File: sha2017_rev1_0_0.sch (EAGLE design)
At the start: 205 parts, among them IC1 CP210X_USB_UART, IC2 AP7215, IC3 ESP32WROOM32, IC4 TP4056, IC5 FXL6408, IC6 CPT112, M1 MOTOR10MM, Q1 MMBT2222A, Q2 MMBT2222A, Q3 MMBT2222A, Q4 MMBT2222A, Q5 SI1304 BDL, Q6 MMBT2222A, T1 MOSFET-PCHANNEL, T2 MOSFET-PCHANNEL, T3 MOSFET-PCHANNEL, X2 2908-05WB-MG, X4 JST-PH3

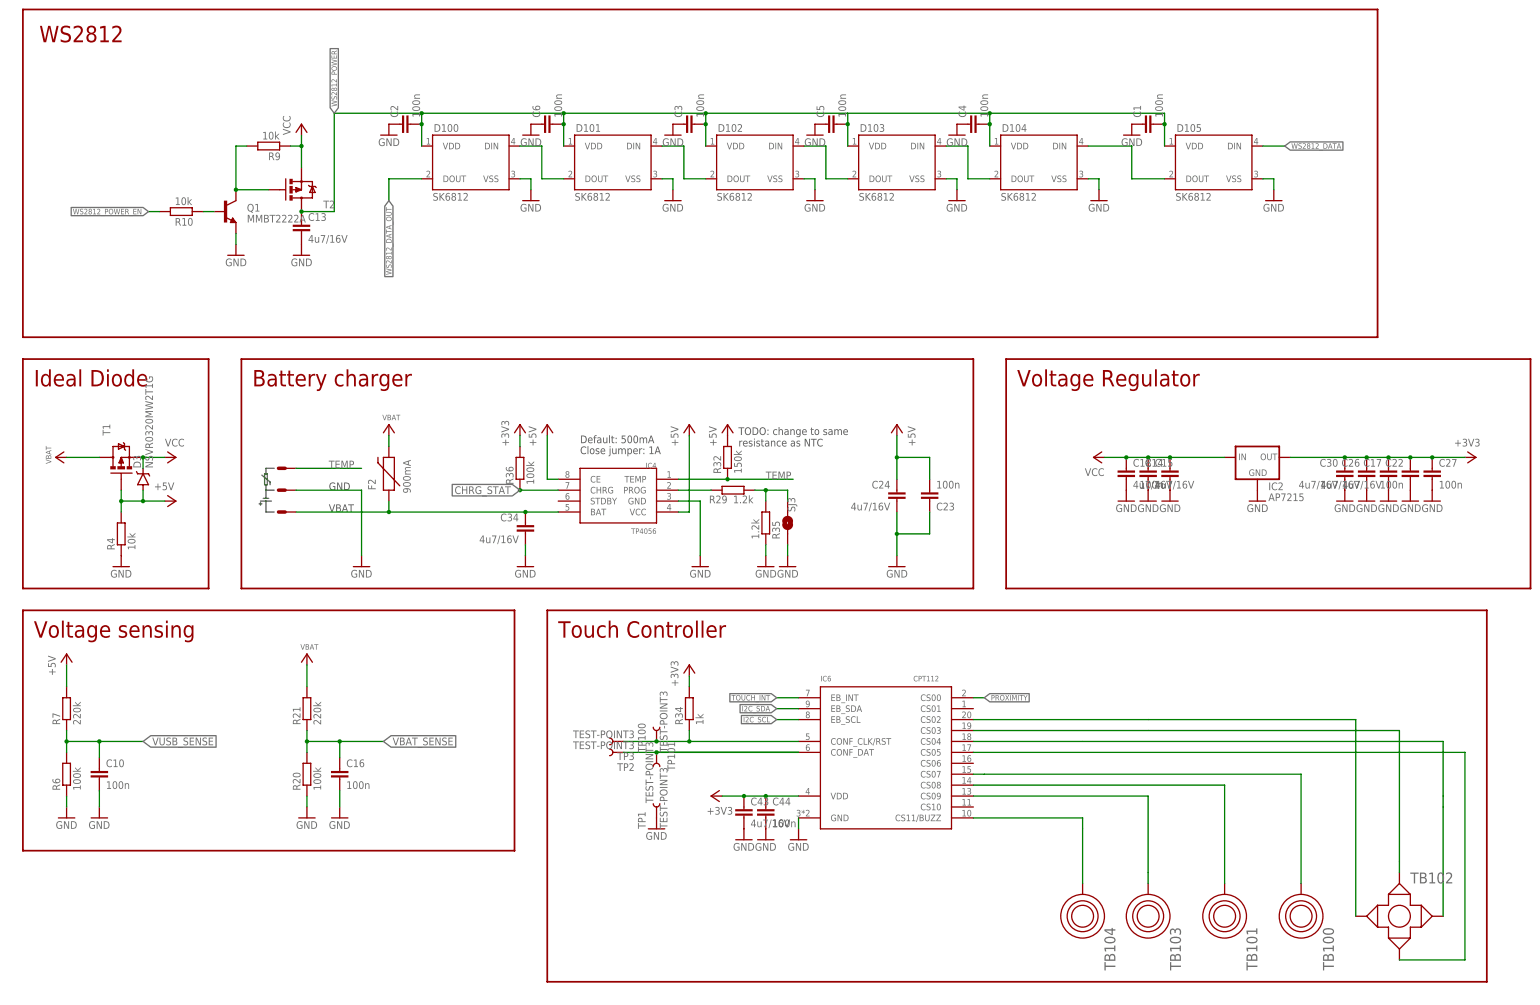
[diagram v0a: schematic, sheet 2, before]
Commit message: Swap port expander and CPT112S for MPR121
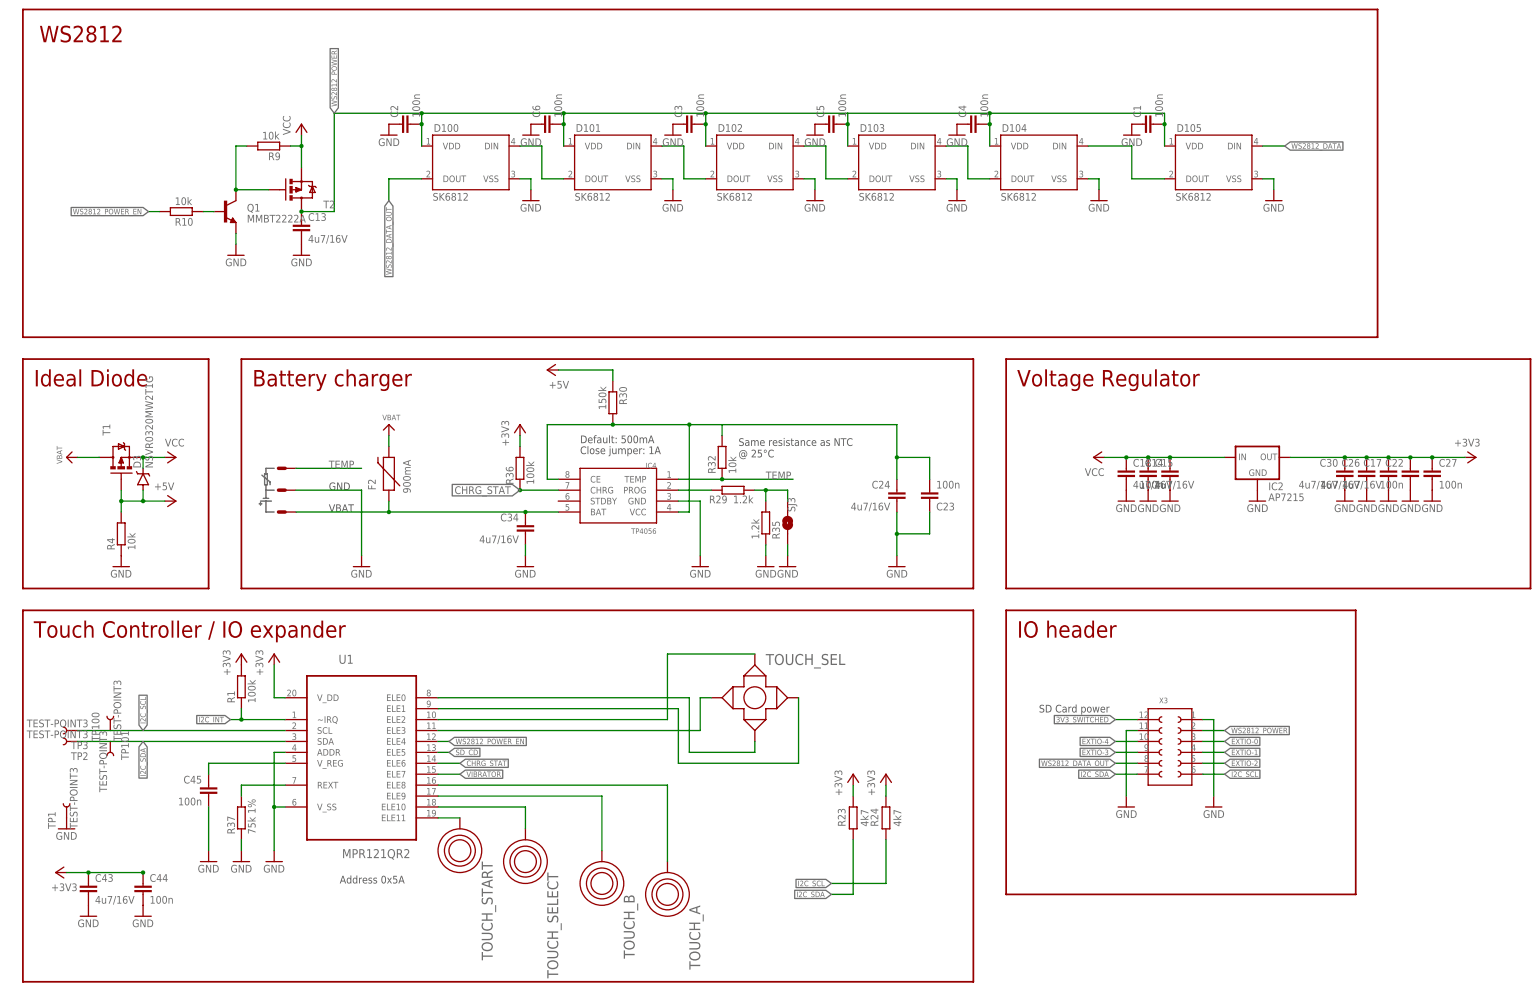
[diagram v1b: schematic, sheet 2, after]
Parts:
- removed C42: 100n, sha2017_rev0_1_0_dev:C0603-DASHES
- removed IC5: FXL6408, badge:FXL6408
- removed IC6: CPT112, badge:CPT112
- removed R26, R33: 10k, sha2017_rev0_1_0_dev:R0603-DASHES
- removed R34: 1k, sha2017_rev0_1_0_dev:R0603-DASHES
- removed SJ1, SJ2: JUMPER-PAD-2-NOYES_SILK, SparkFun-Passives:JUMPER-PAD-2-NOYES_SILK
- removed TB100, TB101: TOUCHSELECT, badge:TOUCHSELECT
- removed TB102: TOUCH_CROSS, badge:TOUCH_CROSS
- removed TB103, TB104: TOUCHROUND, badge:TOUCHROUND
- added C45: 100n, sha2017_rev0_1_0_dev:C0603-DASHES
- added R30: 150k, sha2017_rev0_1_0_dev:R0603-DASHES
- added R37: 75k 1%, sha2017_rev0_1_0_dev:R0603-DASHES
- added TOUCH_A, TOUCH_B: TOUCHROUND, badge:TOUCHROUND
- added TOUCH_SEL: TOUCH_CROSS, badge:TOUCH_CROSS
- added TOUCH_SELECT, TOUCH_START: TOUCHSELECT, badge:TOUCHSELECT
- added U1: MPR121QR2, Freescale_By_element14_Batch_1:MPR121QR2
- R1: value 10k -> 100k; device 00ralf:R0603-DASHES -> sha2017_rev0_1_0_dev:R0603-DASHES; PARTNO ERJ-3GEYJ103V -> ERJ-3GEYJ104V
- R32: value 150k -> 10k
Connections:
- removed net EXTIO-5: IC5.GPIO5, X3.2
- removed net N$55: IC6.CS03, TB102.UP
- removed net N$57: IC6.CS05, TB102.DOWN
- removed net N$58: IC6.CS09, TB103.P$1
- removed net N$59: IC5.!RESET, R33.2
- removed net N$61: IC6.CONF_CLK/RST, R34.1, TP100.1, TP3.1
- removed net N$62: IC6.CONF_DAT, TP101.1, TP2.1
- removed net N$64: IC6.CS08, TB101.P$1
- removed net N$65: IC6.CS07, TB100.P$1
- removed net PROXIMITY: IC6.CS00
- removed net SD_DATA1: IC3.IO4, R1.1, SJ2.1
- removed net SD_DATA2: IC3.IO12, SJ1.1
- removed net SD_DATA2_OUT: R26.1, SJ1.2, X2.NC
- removed net TOUCH_INT: IC5.GPIO3, IC6.EB_INT
- new net N$12: C23.2, C24.1, IC4.CE, IC4.VCC, R30.2, R32.2
- new net N$20: C45.1, U1.V_REG
- new net N$21: R37.2, U1.REXT
- new net N$24: TOUCH_B.P$1, U1.ELE9
- new net N$44: TOUCH_SEL.DOWN, U1.ELE0
- new net N$46: TOUCH_SELECT.P$1, U1.ELE10
- new net N$47: TOUCH_SEL.UP, U1.ELE2
- net +3V3: now also R1.2, U1.V_DD; no longer C42.1, IC5.ADDR, IC5.VCC, IC5.VDDIO, IC6.VDD, R33.1, R34.2
- net +5V: now also R30.1; no longer C23.2, C24.1, IC4.CE, IC4.VCC, R32.2
- net 3V3_SWITCHED: no longer R1.2, R26.2
- net CHRG_STAT: now also U1.ELE6; no longer IC5.GPIO0
- net EXTIO-3: now also IC3.IO4; no longer IC5.GPIO7
- net EXTIO-4: now also IC3.IO12; no longer IC5.GPIO6
- net GND: now also C45.2, R37.1, U1.ADDR, U1.V_SS, X3.2; no longer C42.2, IC5.GND, IC6.GND
- net I2C_INT: now also R1.1, U1.~IRQ; no longer IC5.INT
- net I2C_SCL: now also TP100.1, TP3.1, U1.SCL; no longer IC5.SCL, IC6.EB_SCL
- net I2C_SDA: now also TP101.1, TP2.1, U1.SDA; no longer IC5.SDA, IC6.EB_SDA
- net N$1: now also TOUCH_A.P$1, U1.ELE8; no longer IC6.CS11/BUZZ, TB104.P$1
- net N$25: now also TOUCH_SEL.LEFT, U1.ELE3; no longer IC6.CS02, TB102.LEFT
- net N$56: now also TOUCH_SEL.RIGHT, U1.ELE1; no longer IC6.CS04, TB102.RIGHT
- net N$6: now also TOUCH_START.P$1, U1.ELE11; no longer SJ2.2, X2.RSV
- net SD_CD: now also U1.ELE5; no longer IC5.GPIO4
- net VIBRATOR: now also U1.ELE7; no longer IC5.GPIO1
- net WS2812_POWER_EN: now also U1.ELE4; no longer IC5.GPIO2
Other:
- note added: "Address 0x5A"
- note added: "DAT1"
- note added: "DAT2"
- note added: "SD Card power"
- note added: "Same resistance as NTC @ 25°C"
- note added: "Touch Controller / IO expander"
- note removed: "Port Expander"
- note removed: "TODO: change to same resistance as NTC"
- note removed: "Touch Controller"
- moved on the sheet: C43, C44, M1, Q2, R11, R2, R31, R32, TP1, TP100, TP101, TP2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

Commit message: Replace BJTs by AO3400 nFET
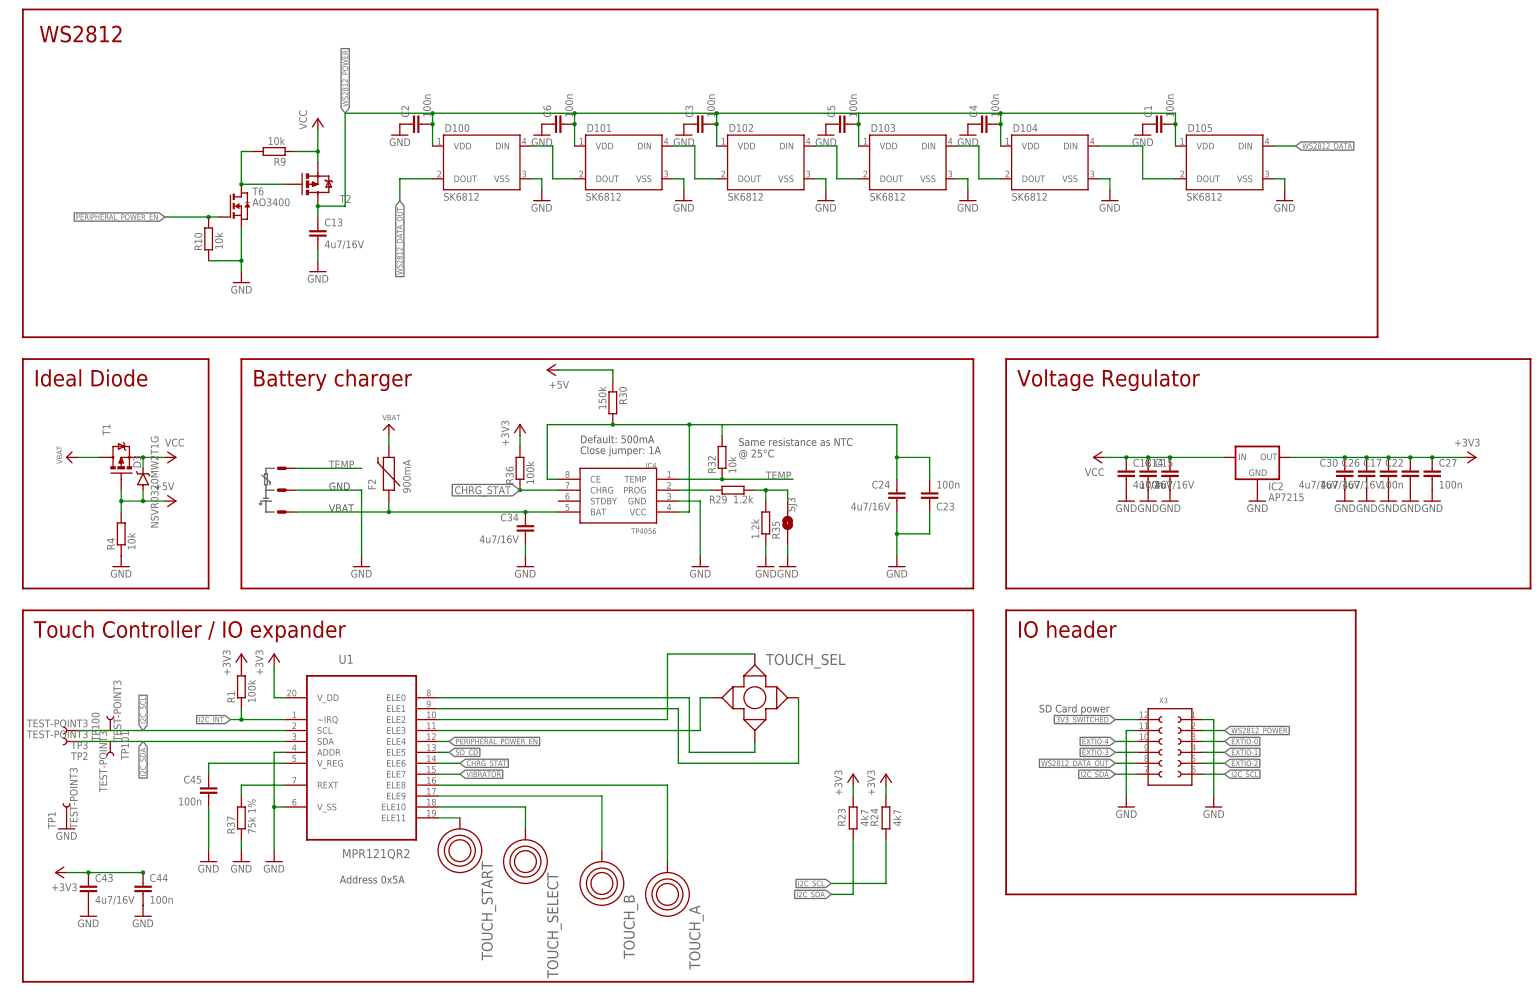
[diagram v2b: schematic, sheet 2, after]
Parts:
- removed Q1, Q2, Q6: MMBT2222A, SparkFun-DiscreteSemi:TRANSISTOR_NPNMMBT2222A
- added T4, T5, T6: AO3400, zetex:NMOSSOT23
- R11, R27: value 10k -> 100k
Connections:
- removed net N$15: Q6.B, R27.2
- removed net N$45: Q2.B, R11.1
- removed net N$52: Q1.B, R10.2
- removed net WS2812_POWER_EN: R10.1, R27.1, U1.ELE4
- new net PERIPHERAL_POWER_EN: R10.1, R27.2, T5.G, T6.G, U1.ELE4
- net GND: now also R10.2, R11.2, R27.1, T4.S, T5.S, T6.S; no longer Q1.E, Q2.E, Q6.E
- net N$16: now also T4.D; no longer Q2.C
- net N$17: now also T5.D; no longer Q6.C
- net N$53: now also T6.D; no longer Q1.C
- net VIBRATOR: now also R11.1, T4.G; no longer R11.2
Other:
- moved on the sheet: C1, C13, C2, C3, C4, C5, C6, D100, D101, D102, D103, D104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

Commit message: Fix r10
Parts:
- R4: value 10k -> 100k
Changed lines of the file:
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@@
 <setting verticaltext="up"/>
 </settings>
-<grid distance="0.05" unitdist="inch" unit="inch" style="lines" multiple="1" display="no" altdistance="0.01" altunitdist="inch" altunit="inch"/>
+<grid distance="0.1" unitdist="inch" unit="inch" style="lines" multiple="1" display="no" altdistance="0.01" altunitdist="inch" altunit="inch"/>
 <layers>
-<layer number="1" name="Top" color="4" fill="1" visible="yes" active="no"/>
-<layer number="2" name="Route2" color="1" fill="3" visible="yes" active="no"/>
-<layer number="3" name="Route3" color="4" fill="3" visible="yes" active="no"/>
-<layer number="4" name="Route4" color="1" fill="4" visible="yes" active="no"/>
-<layer number="5" name="Route5" color="4" fill="4" visible="yes" active="no"/>
-<layer number="6" name="Route6" color="1" fill="8" visible="yes" active="no"/>
-<layer number="7" name="Route7" color="4" fill="8" visible="yes" active="no"/>
-<layer number="8" name="Route8" color="1" fill="2" visible="yes" active="no"/>
-<layer number="9" name="Route9" color="4" fill="2" visible="yes" active="no"/>
-<layer number="10" name="Route10" color="1" fill="7" visible="yes" active="no"/>
-<layer number="11" name="Route11" color="4" fill="7" visible="yes" active="no"/>
-<layer number="12" name="Route12" color="1" fill="5" visible="yes" active="no"/>
-<layer number="13" name="Route13" color="4" fill="5" visible="yes" active="no"/>
-<layer number="14" name="Route14" color="1" fill="6" visible="yes" active="no"/>
-<layer number="15" name="Route15" color="4" fill="6" visible="yes" active="no"/>
-<layer number="16" name="Bottom" color="1" fill="1" visible="yes" active="no"/>
-<layer number="17" name="Pads" color="2" fill="1" visible="yes" active="no"/>
-<layer number="18" name="Vias" color="2" fill="1" visible="yes" active="no"/>
-<layer number="19" name="Unrouted" color="6" fill="1" visible="yes" active="no"/>
-<layer number="20" name="Dimension" color="15" fill="1" visible="yes" active="no"/>
-<layer number="21" name="tPlace" color="7" fill="1" visible="yes" active="no"/>
-<layer number="22" name="bPlace" color="7" fill="1" visible="yes" active="no"/>
-<layer number="23" name="tOrigins" color="15" fill="1" visible="yes" active="no"/>
-<layer number="24" name="bOrigins" color="15" fill="1" visible="yes" active="no"/>
-<layer number="25" name="tNames" color="7" fill="1" visible="yes" active="no"/>
-<layer number="26" name="bNames" color="7" fill="1" visible="yes" active="no"/>
-<layer number="27" name="tValues" color="7" fill="1" visible="yes" active="no"/>
-<layer number="28" name="bValues" color="7" fill="1" visible="yes" active="no"/>
+<layer number="1" name="Top" color="4" fill="1" visible="no" active="no"/>
+<layer number="2" name="Route2" color="1" fill="3" visible="no" active="no"/>
+<layer number="3" name="Route3" color="4" fill="3" visible="no" active="no"/>
+<layer number="4" name="Route4" color="1" fill="4" visible="no" active="no"/>
+<layer number="5" name="Route5" color="4" fill="4" visible="no" active="no"/>
+<layer number="6" name="Route6" color="1" fill="8" visible="no" active="no"/>
+<layer number="7" name="Route7" color="4" fill="8" visible="no" active="no"/>
+<layer number="8" name="Route8" color="1" fill="2" visible="no" active="no"/>
+<layer number="9" name="Route9" color="4" fill="2" visible="no" active="no"/>
+<layer number="10" name="Route10" color="1" fill="7" visible="no" active="no"/>
+<layer number="11" name="Route11" color="4" fill="7" visible="no" active="no"/>
+<layer number="12" name="Route12" color="1" fill="5" visible="no" active="no"/>
+<layer number="13" name="Route13" color="4" fill="5" visible="no" active="no"/>
+<layer number="14" name="Route14" color="1" fill="6" visible="no" active="no"/>
+<layer number="15" name="Route15" color="4" fill="6" visible="no" active="no"/>
+<layer number="16" name="Bottom" color="1" fill="1" visible="no" active="no"/>
+<layer number="17" name="Pads" color="2" fill="1" visible="no" active="no"/>
+<layer number="18" name="Vias" color="2" fill="1" visible="no" active="no"/>
+<layer number="19" name="Unrouted" color="6" fill="1" visible="no" active="no"/>
+<layer number="20" name="Dimension" color="15" fill="1" visible="no" active="no"/>
+<layer number="21" name="tPlace" color="7" fill="1" visible="no" active="no"/>
+<layer number="22" name="bPlace" color="7" fill="1" visible="no" active="no"/>
+<layer number="23" name="tOrigins" color="15" fill="1" visible="no" active="no"/>
+<layer number="24" name="bOrigins" color="15" fill="1" visible="no" active="no"/>
+<layer number="25" name="tNames" color="7" fill="1" visible="no" active="no"/>
+<layer number="26" name="bNames" color="7" fill="1" visible="no" active="no"/>
+<layer number="27" name="tValues" color="7" fill="1" visible="no" active="no"/>
+<layer number="28" name="bValues" color="7" fill="1" visible="no" active="no"/>
 <layer number="29" name="tStop" color="7" fill="3" visible="no" active="no"/>
 <layer number="30" name="bStop" color="7" fill="6" visible="no" active="no"/>
@@
 <layer number="35" name="tGlue" color="7" fill="4" visible="no" active="no"/>
 <layer number="36" name="bGlue" color="7" fill="5" visible="no" active="no"/>
-<layer number="37" name="tTest" color="7" fill="1" visible="yes" active="no"/>
-<layer number="38" name="bTest" color="7" fill="1" visible="yes" active="no"/>
+<layer number="37" name="tTest" color="7" fill="1" visible="no" active="no"/>
+<layer number="38" name="bTest" color="7" fill="1" visible="no" active="no"/>
 <layer number="39" name="tKeepout" color="4" fill="11" visible="no" active="no"/>
 <layer number="40" name="bKeepout" color="1" fill="11" visible="no" active="no"/>
@@
 <layer number="44" name="Drills" color="7" fill="1" visible="no" active="no"/>
 <layer number="45" name="Holes" color="7" fill="1" visible="no" active="no"/>
-<layer number="46" name="Milling" color="3" fill="1" visible="yes" active="no"/>
-<layer number="47" name="Measures" color="7" fill="1" visible="yes" active="no"/>
-<layer number="48" name="Document" color="7" fill="1" visible="yes" active="no"/>
-<layer number="49" name="Reference" color="7" fill="1" visible="yes" active="no"/>
-<layer number="50" name="dxf" color="7" fill="1" visible="yes" active="no"/>
-<layer number="51" name="tDocu" color="7" fill="1" visible="yes" active="no"/>
-<layer number="52" name="bDocu" color="7" fill="1" visible="yes" active="no"/>
-<layer number="53" name="tGND_GNDA" color="7" fill="9" visible="yes" active="no"/>
-<layer number="54" name="bGND_GNDA" color="1" fill="9" visible="yes" active="no"/>
-<layer number="56" name="wert" color="7" fill="1" visible="yes" active="no"/>
-<layer number="57" name="tCAD" color="7" fill="1" visible="yes" active="no"/>
-<layer number="58" name="bCAD" color="11" fill="1" visible="yes" active="no"/>
-<layer number="59" name="tCarbon" color="7" fill="1" visible="yes" active="no"/>
-<layer number="60" name="bCarbon" color="7" fill="1" visible="yes" active="no"/>
-<layer number="61" name="stand" color="7" fill="1" visible="yes" active="no"/>
+<layer number="46" name="Milling" color="3" fill="1" visible="no" active="no"/>
+<layer number="47" name="Measures" color="7" fill="1" visible="no" active="no"/>
+<layer number="48" name="Document" color="7" fill="1" visible="no" active="no"/>
+<layer number="49" name="Reference" color="7" fill="1" visible="no" active="no"/>
+<layer number="50" name="dxf" color="7" fill="1" visible="no" active="no"/>
+<layer number="51" name="tDocu" color="7" fill="1" visible="no" active="no"/>
+<layer number="52" name="bDocu" color="7" fill="1" visible="no" active="no"/>
+<layer number="53" name="tGND_GNDA" color="7" fill="9" visible="no" active="no"/>
+<layer number="54" name="bGND_GNDA" color="1" fill="9" visible="no" active="no"/>
+<layer number="56" name="wert" color="7" fill="1" visible="no" active="no"/>
+<layer number="57" name="tCAD" color="7" fill="1" visible="no" active="no"/>
+<layer number="58" name="bCAD" color="11" fill="1" visible="no" active="no"/>
+<layer number="59" name="tCarbon" color="7" fill="1" visible="no" active="no"/>
+<layer number="60" name="bCarbon" color="7" fill="1" visible="no" active="no"/>
+<layer number="61" name="stand" color="7" fill="1" visible="no" active="no"/>
 <layer number="90" name="Modules" color="5" fill="1" visible="yes" active="yes"/>
 <layer number="91" name="Nets" color="2" fill="1" visible="yes" active="yes"/>
@@
 <attribute name="PARTNO" value=""/>
 </part>
-<part name="R4" library="sha2017_rev0_1_0_dev" deviceset="R0603-DASHES" device="" value="10k">
-<attribute name="PARTNO" value="ERJ-3GEYJ103V"/>
-</part>
+<part name="R4" library="sha2017_rev0_1_0_dev" deviceset="R0603-DASHES" device="" value="100k">
+<attribute name="PARTNO" value="ERJ-3GEYJ103V"/>
+</part>
